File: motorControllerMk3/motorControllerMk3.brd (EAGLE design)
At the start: 100 x 80 mm, 39 parts, among them IC1 VNH3SP30, IC2 VNH3SP30

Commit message: deleted useless files, playing around with layout
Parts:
- moved R3 157.1 mm to (88.9, 6.35)
- moved SV2 146.4 mm to (87.6, 34.3)
- moved CN1 145.0 mm to (94.0, 72.4)
- moved R2 145.0 mm to (81.3, 6.35)
- moved C7 140.3 mm to (78.7, 72.4)
- moved C5 135.4 mm to (73.7, 6.35)
- moved C1 134.1 mm to (68.6, 73.7)
- moved C6 133.6 mm to (77.5, 50.8)
- moved LED5 124.1 mm to (68.6, 49.5)
- moved SV1 119.4 mm to (77.5, 43.2), turned to 180 degrees
- moved IC1 97.2 mm to (72.4, 21.6), turned to 270 degrees
- moved LED6 94.5 mm to (33.0, 74.9)
- moved R11 90.9 mm to (39.4, 64.8)
- moved Q1 85.6 mm to (52.1, 73.7)
- moved U$1 80.0 mm to (48.3, 44.5), turned to 180 degrees
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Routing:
- net +12V: track 0.00 -> 55.2 mm

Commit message: further layouting
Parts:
- moved R17 96.8 mm to (45.7, 21.6)
- moved R14 95.6 mm to (59.7, 21.6), turned to 180 degrees
- moved R13 92.7 mm to (59.7, 16.5), turned to 180 degrees
- moved R16 90.4 mm to (45.7, 26.7)
- moved R15 89.2 mm to (45.7, 16.5)
- moved R12 84.3 mm to (59.7, 26.7), turned to 180 degrees
- moved R5 75.0 mm to (45.7, 24.1)
- moved R10 73.8 mm to (58.4, 58.4)
- moved R4 73.3 mm to (45.7, 19.1)
- moved R3 31.9 mm to (59.7, 19.1), turned to 180 degrees
- moved R2 28.0 mm to (59.7, 24.1), turned to 180 degrees
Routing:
- net +5V: track 0.00 -> 25.4 mm, vias 0 -> 4
- net N$25: track 0.00 -> 18.1 mm
- net N$24: track 0.00 -> 18.1 mm
- net N$9: track 0.00 -> 12.4 mm
- net N$8: track 0.00 -> 12.4 mm
- net N$26: track 0.00 -> 6.04 mm
- net N$23: track 0.00 -> 6.03 mm
- net N$36: track 0.00 -> 3.80 mm
- net N$32: track 0.00 -> 3.80 mm
- net N$35: track 0.00 -> 3.80 mm
- net N$33: track 0.00 -> 3.80 mm
- net N$21: track 0.00 -> 2.97 mm
- net N$20: track 0.00 -> 2.97 mm
- net N$19: track 0.00 -> 2.97 mm
- net N$18: track 0.00 -> 2.97 mm
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
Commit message: finished layout
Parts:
- moved LED3 109.5 mm to (62.9, 33.0), turned to 180 degrees
- moved LED2 102.3 mm to (62.9, 36.8), turned to 180 degrees
- moved C4 102.3 mm to (56.5, 55.9)
- moved R9 100.6 mm to (57.1, 36.2), turned to 180 degrees
- moved R7 91.4 mm to (57.1, 33.7)
- moved R8 83.5 mm to (43.8, 33.7), turned to 180 degrees
- moved C7 74.3 mm to (36.2, 11.4), turned to 180 degrees
- moved R6 72.9 mm to (43.8, 36.8)
- moved LED1 72.9 mm to (38.1, 36.8)
- moved C3 70.1 mm to (50.2, 55.2)
- moved SV2 63.6 mm to (24.1, 38.1), turned to 270 degrees
- moved R1 57.4 mm to (33.0, 51.4)
- moved ISP1 55.3 mm to (37.5, 56.5), turned to 90 degrees
- moved C2 53.8 mm to (35.6, 48.3), turned to 90 degrees
- moved LED4 48.6 mm to (38.1, 33.0)
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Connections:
- net N$15: now also SV2.6; no longer SV2.5
- net N$16: now also SV2.5; no longer SV2.6
- net N$24: now also R12.2, U$1.28; no longer R15.2, U$1.22
- net N$25: now also R15.2; no longer R13.2
- net N$26: now also R13.2; no longer R12.2
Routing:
- net +5V: track 25.4 -> 166.6 mm, vias 4 -> 6
- net N$14: track 0.00 -> 36.2 mm, vias 0 -> 3
- net N$16: track 0.00 -> 36.2 mm, vias 0 -> 3
- net N$26: track 6.04 -> 42.2 mm
- net N$17: track 0.00 -> 31.9 mm, vias 0 -> 1
- net GND: track 0.00 -> 25.7 mm, vias 0 -> 1
- net N$12: track 0.00 -> 24.3 mm
- net N$5: track 0.00 -> 20.4 mm, vias 0 -> 1
- net +12V: track 55.2 -> 73.2 mm
- net N$25: track 18.1 -> 35.2 mm
- net N$1: track 0.00 -> 16.2 mm, vias 0 -> 2
- net N$8: track 12.4 -> 28.1 mm, vias 0 -> 2
- net N$6: track 0.00 -> 15.5 mm
- net N$7: track 0.00 -> 15.2 mm
- net N$9: track 12.4 -> 26.8 mm, vias 0 -> 2
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- added copper zone on layer 1, net GND
- added copper zone on layer 16, net GND
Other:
- board size 100 x 80 mm -> 61.3 x 63.5 mm

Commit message: finalizing layout
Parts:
- added S1: (no value), switch-omron:B3F-10XX
- moved C8 34.7 mm to (30.8, 37.8), turned to 90 degrees
- moved C4 8.26 mm to (64.1, 52.7)
- moved CN1 8.03 mm to (60.3, 59.7)
- moved ISP1 3.81 mm to (41.3, 56.5)
- moved LED6 1.91 mm to (69.2, 48.3)
- moved R11 1.91 mm to (69.2, 42.5)
- moved C3 1.42 mm to (51.4, 55.9), turned to 90 degrees
- moved C1 1.27 mm to (35.6, 45.7), turned to 0 degrees
- moved LED5 1.27 mm to (65.4, 48.3)
- moved R10 1.27 mm to (65.4, 42.5)
- moved C2 0.63 mm to (35.6, 47.6), turned to 180 degrees
- moved C7 0.63 mm to (35.6, 11.4)
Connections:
- removed net N$5: ISP1.5, R1.2, U$1.13
- new net N$38: ISP1.5, R1.2, S1.1, S1.2, U$1.13
- net GND: now also S1.3, S1.4
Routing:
- net N$38: track 0.00 -> 33.0 mm, vias 0 -> 1
- net N$5: track 20.4 -> 0.00 mm, vias 1 -> 0
- net +12V: track 73.2 -> 87.7 mm
- net +5V: track 166.6 -> 172.8 mm
- net N$6: track 15.5 -> 10.7 mm
- net N$10: track 6.78 -> 11.4 mm
- net N$11: track 6.78 -> 11.4 mm
- net N$7: track 15.2 -> 11.1 mm
- net N$1: track 16.2 -> 12.4 mm
- net N$4: track 4.67 -> 3.36 mm
- net N$2: track 11.6 -> 10.5 mm
- net N$12: track 24.3 -> 23.3 mm
- net N$3: track 11.4 -> 10.5 mm
- net GND: vias 1 -> 16
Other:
- board size 61.3 x 63.5 mm -> 61.6 x 54.6 mm

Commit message: finalizing layout
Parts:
- removed CN1: (no value), adafruit:USB-MINIB
- removed IC1, IC2: VNH3SP30, st-microelectronics:MULTIPOWERSO-30
- removed ISP1: AVRISP-6, adafruit:AVRISP
- removed Q1: (no value), adafruit:HC49U-V
- removed S1: (no value), switch-omron:B3F-10XX
- removed SV1, SV2: (no value), con-lstb:MA06-1
- added C9: 2200u, rcl:E5-8,5
- added J1: AVR_SPI_PRG_6NS, SparkFun-Connectors:2X3-NS
- added JP1, JP2: (no value), SparkFun-Connectors:1X06
- added JP3: USB-SMD-NS, SparkFun-Connectors:USB-MINIB-NOSTOP
- added S2: SWITCH-MOMENTARY-2PTH, SparkFun-Electromechanical:TACTILE-PTH
- added U$2: ATMEGA32U4TQFP, SparkFun-DigitalIC:SPARKFUN-DIGITALIC_TQFP44
- added U$3: VNH2SP30, SparkFun-PowerIC:VNH2SP30
- added Y1: (no value), SparkFun-FreqCtrl:HC49US
- C1, C2, C3, C4, C5, C6, C7: device rcl:C0805K -> SparkFun-Passives:0805
- LED1: value (none) -> A2; device led:SML1206 -> SparkFun-LED:LED-1206
- LED2: value (none) -> B1; device led:SML1206 -> SparkFun-LED:LED-1206
- LED3: value (none) -> A1; device led:SML1206 -> SparkFun-LED:LED-1206
- LED4: value (none) -> B2; device led:SML1206 -> SparkFun-LED:LED-1206
- LED5: value (none) -> +5V; device led:SML1206 -> SparkFun-LED:LED-1206
- LED6: value (none) -> +12V; device led:SML1206 -> SparkFun-LED:LED-1206
- R1: value (none) -> 10k; device rcl:M0805 -> SparkFun-Passives:0805
- R10, R11, R12, R13, R14, R15, R16, R17, R2, R3, R4, R5, R6, R7, R8, R9: device rcl:M0805 -> SparkFun-Passives:0805
- U$1: value ATMEGA32U4-AU -> VNH2SP30; device adafruit:TQFP44 -> SparkFun-PowerIC:VNH2SP30
- moved U$1 30.0 mm to (33.7, 21.6), turned to 90 degrees
- moved LED6 9.53 mm to (74.9, 55.9), turned to 90 degrees
- moved LED5 9.16 mm to (70.5, 55.9), turned to 90 degrees
- moved R10 8.25 mm to (68.6, 50.2)
- moved R11 8.25 mm to (72.4, 50.2)
- moved R1 3.42 mm to (36.2, 52.7), turned to 270 degrees
- moved C5 3.18 mm to (61.0, 42.5), turned to 0 degrees
- moved LED1 1.91 mm to (40.0, 36.8), turned to 180 degrees
- moved LED2 1.91 mm to (61.0, 36.8), turned to 0 degrees
- moved LED3 1.91 mm to (61.0, 33.0), turned to 0 degrees
- moved LED4 1.91 mm to (40.0, 33.0), turned to 180 degrees
- moved C3 1.42 mm to (52.7, 55.2), turned to 0 degrees
- moved C4 1.27 mm to (64.1, 51.4)
- moved R9 0.90 mm to (56.5, 36.8)
- moved C6 0.64 mm to (64.8, 11.4)
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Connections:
- removed net N$14: IC1.15, IC1.16, IC1.21, IC1.OUTB, IC1.OUTB@1, SV1.5
- removed net N$15: IC2.15, IC2.16, IC2.21, IC2.OUTB, IC2.OUTB@1, SV2.6
- removed net N$16: IC2.1, IC2.25, IC2.30, IC2.OUTA, IC2.OUTA@1, SV2.5
- removed net N$18: IC2.6, R4.1
- removed net N$19: IC2.10, R5.1
- removed net N$21: IC1.10, R3.1
- removed net N$23: R16.2, R8.1, U$1.25
- removed net N$24: R12.2, R7.1, U$1.28
- removed net N$25: R15.2, R6.2, U$1.26
- removed net N$26: R13.2, R9.2, U$1.27
- removed net N$32: IC1.5, R12.1
- removed net N$33: IC1.11, R13.1
- removed net N$34: IC1.8, R14.1
- removed net N$35: IC2.5, R15.1
- removed net N$36: IC2.11, R16.1
- removed net N$37: IC2.8, R17.1
- new net N$5: R16.1, U$1.11
- new net OUTA1: JP1.1, U$3.1, U$3.25, U$3.30, U$3.SLUG3
- new net OUTA2: JP2.2, U$1.1, U$1.25, U$1.30, U$1.SLUG3
- new net OUTB1: JP1.2, U$3.15, U$3.16, U$3.21, U$3.SLUG2
- new net OUTB2: JP2.1, U$1.15, U$1.16, U$1.21, U$1.SLUG2
- new net PB0: U$2.8
- new net PB1: J1.3, U$2.9
- new net PB2: J1.4, U$2.10
- new net PB3: J1.1, U$2.11
- new net PB4: R12.2, R7.1, U$2.28
- new net PB5: R17.2, U$2.29
- new net PB6: R14.2, U$2.30
- new net PB7: U$2.12
- new net PC6: U$2.31
- new net PC7: U$2.32
- new net PD0: JP2.6, U$2.18
- new net PD1: JP1.6, U$2.19
- new net PD2: U$2.20
- new net PD3: U$2.21
- new net PD4: R16.2, R8.1, U$2.25
- new net PD5: U$2.22
- new net PD6: R15.2, R6.2, U$2.26
- new net PD7: R13.2, R9.2, U$2.27
- new net PE6: U$2.1
- net +12V: now also C9.+, U$1.13, U$1.23, U$1.3, U$1.SLUG1, U$3.13, U$3.23, U$3.3, U$3.SLUG1; no longer IC1.13, IC1.23, IC1.3, IC1.VCC, IC1.VCC@1, IC2.13, IC2.23, IC2.3, IC2.VCC, IC2.VCC@1
- net +5V: now also J1.2, JP1.4, JP2.4, JP3.VBUS, U$2.14, U$2.2, U$2.24, U$2.34, U$2.44, U$2.7; no longer CN1.VBUS, ISP1.2, SV1.3, SV2.3, U$1.14, U$1.2, U$1.24, U$1.34, U$1.44, U$1.7
- net GND: now also C9.-, J1.6, JP1.3, JP2.3, JP3.GND, S2.1, U$1.18, U$1.19, U$1.20, U$1.26, U$1.27, U$1.28, U$2.15, U$2.23, U$2.35, U$2.43, U$2.5, U$3.18, U$3.19, U$3.20, U$3.26, U$3.27, U$3.28; no longer CN1.GND, IC1.18, IC1.19, IC1.20, IC1.26, IC1.27, IC1.28, IC2.18, IC2.19, IC2.20, IC2.26, IC2.27, IC2.28, ISP1.6, S1.3, S1.4, SV1.4, SV2.4, U$1.15, U$1.23, U$1.35, U$1.43, U$1.5
- net N$1: now also R15.1, U$1.5; no longer ISP1.3, U$1.9
- net N$10: now also JP3.D+, U$2.4; no longer CN1.D+, U$1.4
- net N$11: now also JP3.D-, U$2.3; no longer CN1.D-, U$1.3
- net N$12: now also R13.1, U$3.11; no longer SV2.1, U$1.18
- net N$13: now also R14.1, U$3.8; no longer IC1.1, IC1.25, IC1.30, IC1.OUTA, IC1.OUTA@1, SV1.6
- net N$17: now also R3.1, U$3.10; no longer SV1.1, U$1.19
- net N$2: now also U$2.16, Y1.1; no longer Q1.1, U$1.16
- net N$20: now also U$3.6; no longer IC1.6
- net N$3: now also U$2.17, Y1.2; no longer Q1.2, U$1.17
- net N$38: now also J1.5, S2.3, U$2.13; no longer ISP1.5, S1.1, S1.2, U$1.13
- net N$4: now also U$2.6; no longer U$1.6
- net N$6: now also R17.1, U$1.8; no longer ISP1.4, U$1.10
- net N$7: now also R5.1, U$1.10; no longer ISP1.1, U$1.11
- net N$8: now also R4.1, U$1.6; no longer R17.2, U$1.29
- net N$9: now also R12.1, U$3.5; no longer R14.2, U$1.30
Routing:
- net OUTA2: track 0.00 -> 85.4 mm, vias 0 -> 6
- net OUTB1: track 0.00 -> 83.7 mm, vias 0 -> 6
- net +12V: track 87.7 -> 166.6 mm, vias 0 -> 4
- net N$26: track 42.2 -> 0.00 mm
- net PD7: track 0.00 -> 41.8 mm
- net OUTB2: track 0.00 -> 39.9 mm
- net OUTA1: track 0.00 -> 39.9 mm
- net N$14: track 36.2 -> 0.00 mm, vias 3 -> 0
- net N$16: track 36.2 -> 0.00 mm, vias 3 -> 0
- net N$25: track 35.2 -> 0.00 mm
- net PD6: track 0.00 -> 35.0 mm
- net PD1: track 0.00 -> 31.0 mm, vias 0 -> 1
- net N$17: track 31.9 -> 2.65 mm, vias 1 -> 0
- net PB5: track 0.00 -> 28.1 mm, vias 0 -> 2
- net PB6: track 0.00 -> 26.8 mm, vias 0 -> 2
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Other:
- board size 61.6 x 54.6 mm -> 57.1 x 52.7 mm
- board text added: "+12V"
- board text added: "GND"
- board text added: "ISP"
- board text added: "RESET"

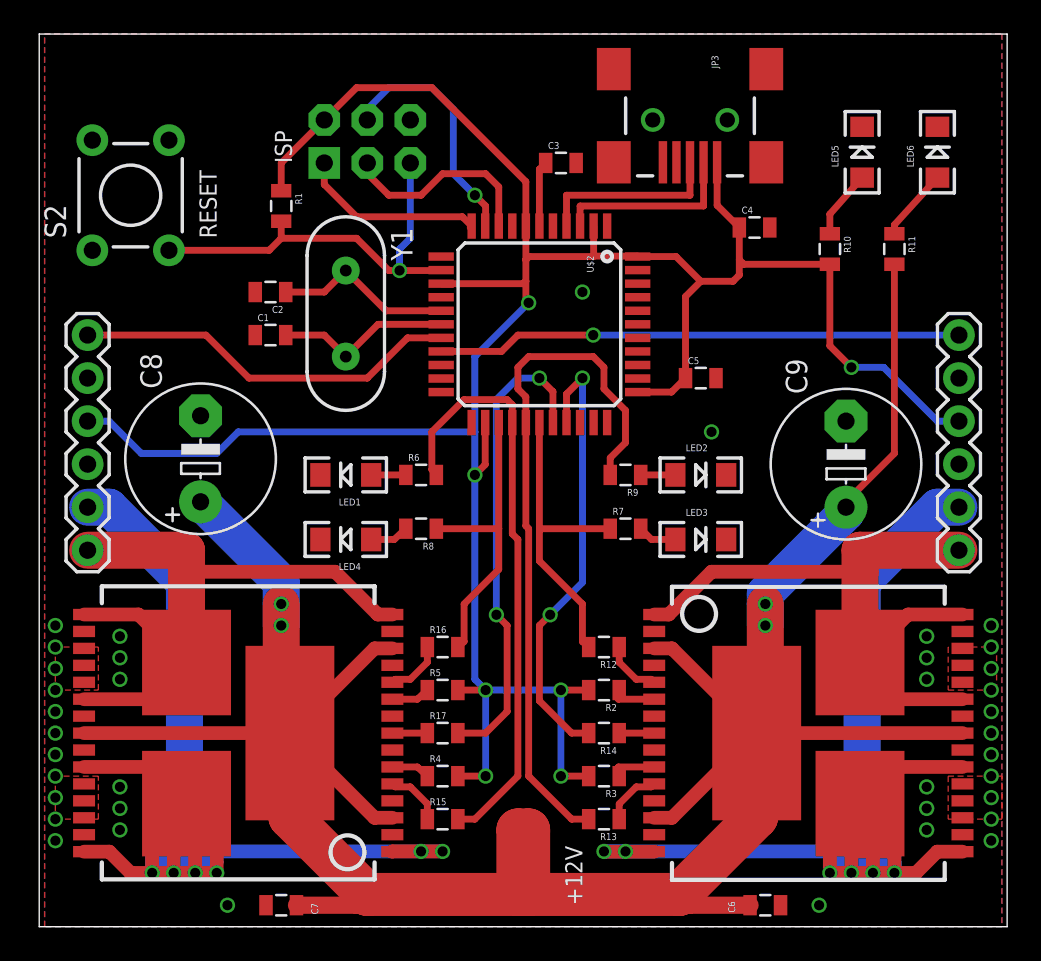
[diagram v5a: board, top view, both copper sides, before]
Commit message: now fits onto 5x10 cm pcb
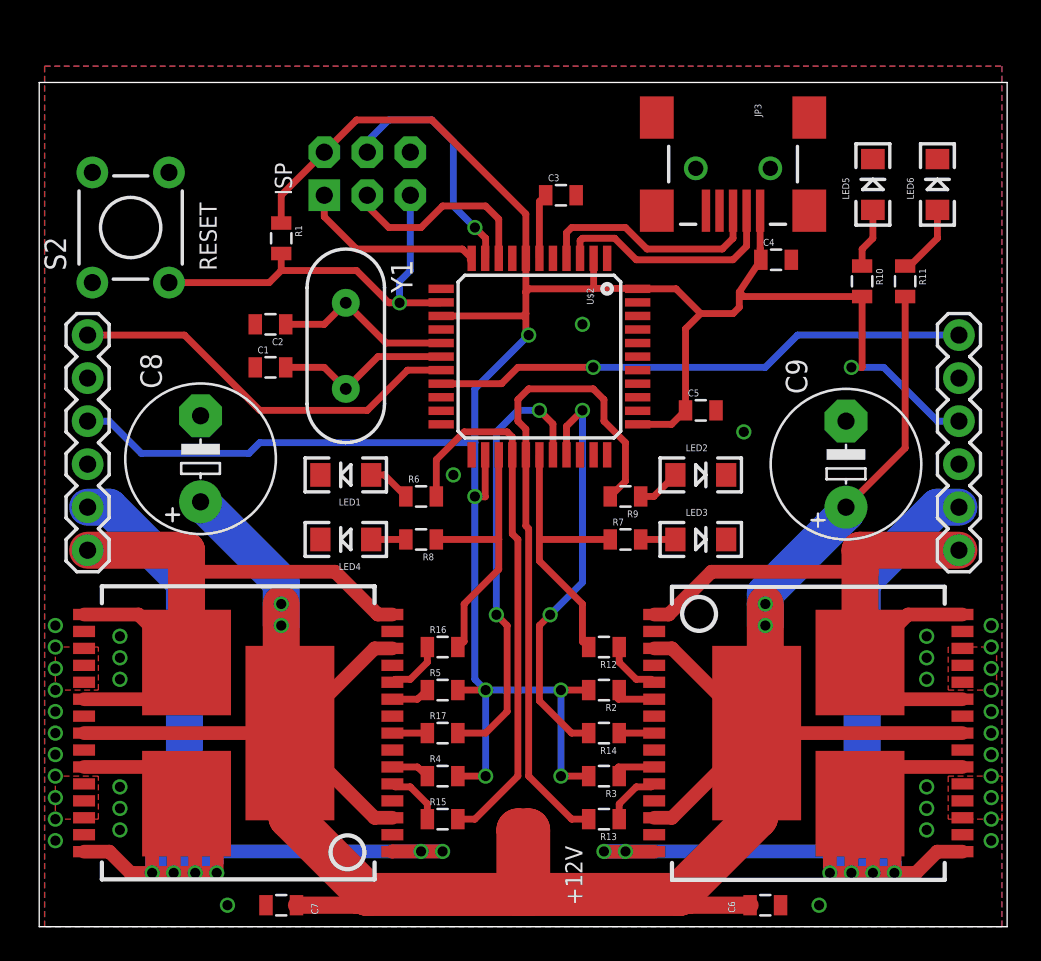
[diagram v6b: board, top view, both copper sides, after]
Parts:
- moved JP3 3.82 mm to (62.9, 54.9)
- moved R10 2.69 mm to (70.5, 48.3)
- moved C4 2.29 mm to (65.4, 49.5)
- moved LED5 2.01 mm to (71.1, 54.0)
- moved R11 2.01 mm to (73.0, 48.3)
- moved C1 1.91 mm to (35.6, 43.2)
- moved C2 1.91 mm to (35.6, 45.7)
- moved C5 1.91 mm to (61.0, 40.6)
- moved J1 1.91 mm to (41.3, 54.6)
- moved LED6 1.91 mm to (74.9, 54.0)
- moved R1 1.91 mm to (36.2, 50.8)
- moved S2 1.91 mm to (27.3, 51.4)
- moved U$2 1.91 mm to (51.4, 43.8)
- moved C3 1.90 mm to (52.7, 53.3)
- moved Y1 1.90 mm to (40.0, 44.5)
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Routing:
- net +5V: track 157.0 -> 153.6 mm
- net N$10: track 11.1 -> 13.9 mm
- net N$11: track 11.1 -> 13.9 mm
- net PD6: track 35.0 -> 32.2 mm
- net PD7: track 41.8 -> 39.3 mm
- net PD4: track 18.0 -> 16.0 mm
- net PB6: track 26.8 -> 24.9 mm
- net PB4: track 18.7 -> 16.7 mm
- net PB5: track 28.1 -> 26.2 mm
- net +12V: track 166.6 -> 165.0 mm
- net PD0: track 22.9 -> 23.7 mm
- net PD1: track 31.0 -> 31.8 mm
- net N$31: track 2.04 -> 2.57 mm
- net N$30: track 2.05 -> 2.57 mm
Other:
- board size 57.1 x 52.7 mm -> 57.1 x 49.8 mm

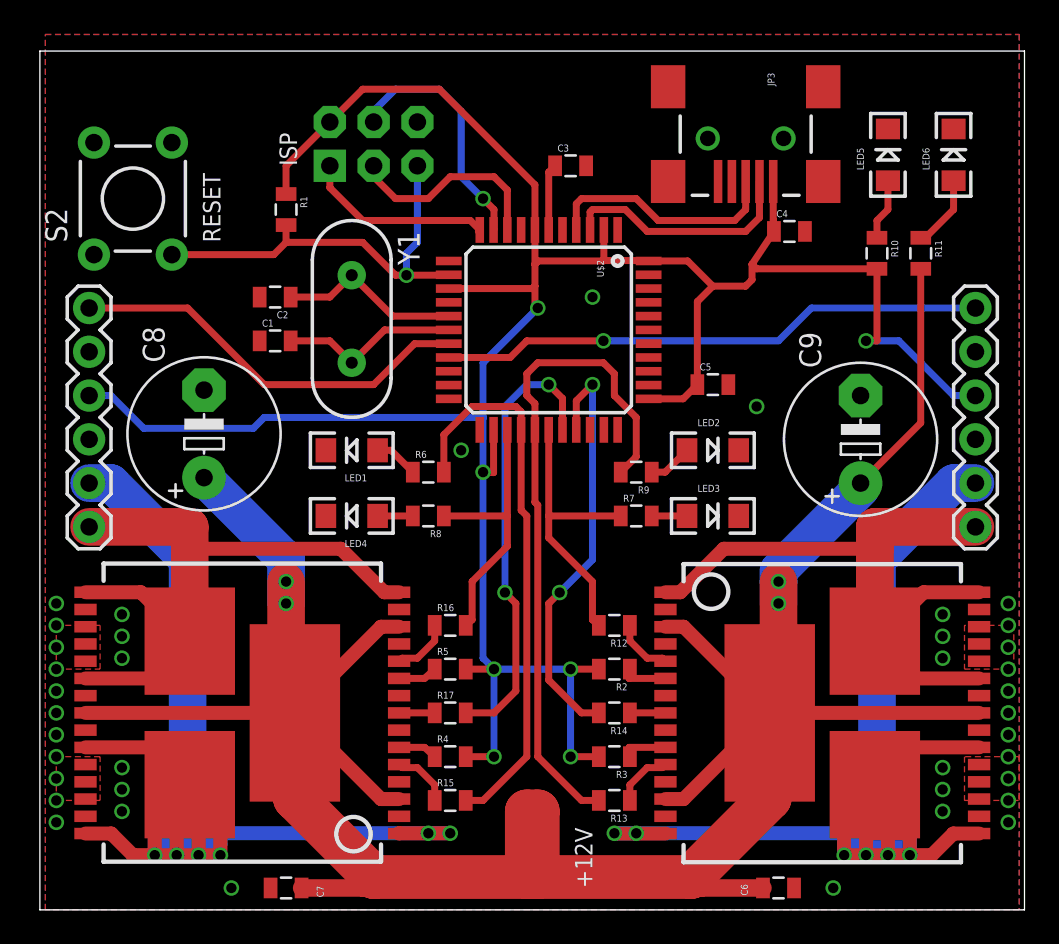
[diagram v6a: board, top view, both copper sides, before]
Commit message: making pcb smaller
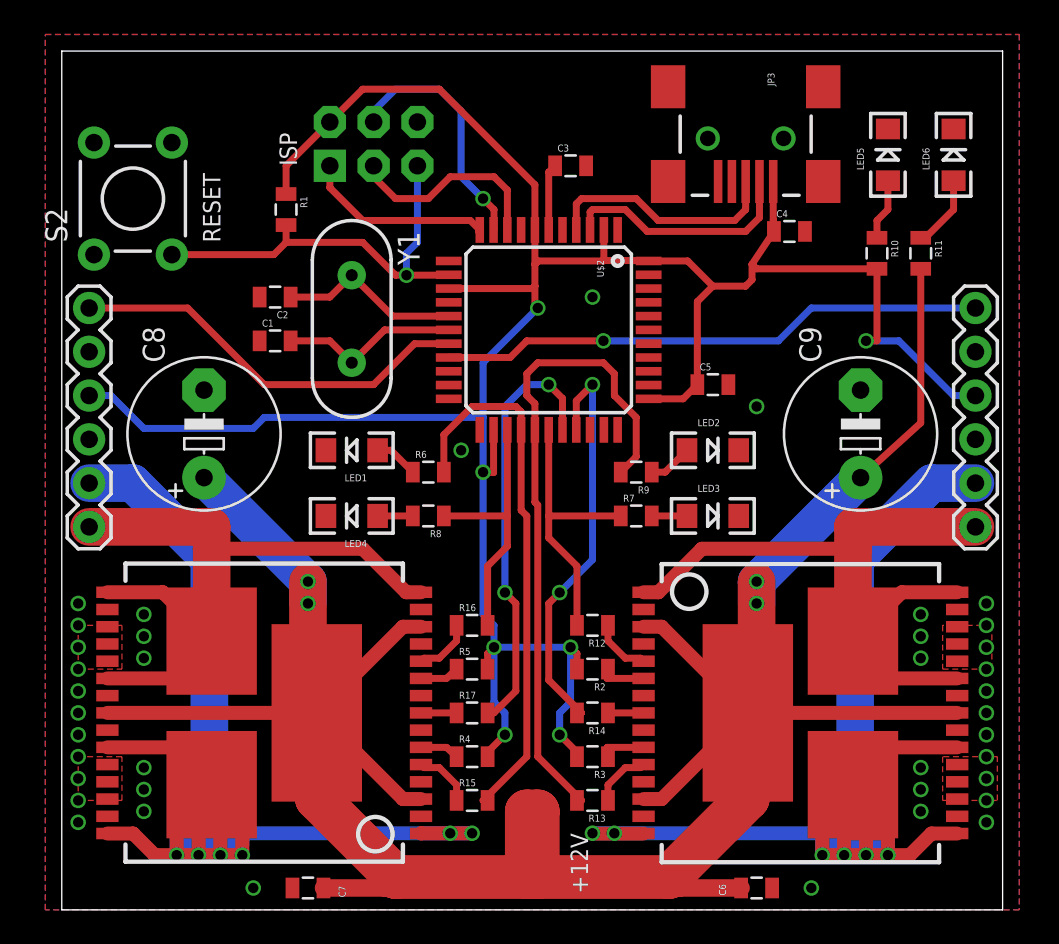
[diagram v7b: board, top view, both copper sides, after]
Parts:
- moved C7 1.27 mm to (37.5, 11.4)
- moved R15 1.27 mm to (47.0, 16.5)
- moved R16 1.27 mm to (47.0, 26.7)
- moved R17 1.27 mm to (47.0, 21.6)
- moved R4 1.27 mm to (47.0, 19.1)
- moved R5 1.27 mm to (47.0, 24.1)
- moved C6 1.27 mm to (63.5, 11.4)
- moved R12 1.27 mm to (54.0, 26.7)
- moved R13 1.27 mm to (54.0, 16.5)
- moved R14 1.27 mm to (54.0, 21.6)
- moved R2 1.27 mm to (54.0, 24.1)
- moved R3 1.27 mm to (54.0, 19.1)
- moved U$1 1.27 mm to (34.9, 21.6)
- moved U$3 1.27 mm to (66.0, 21.6)
- moved C9 0.32 mm to (69.5, 37.8)
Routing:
- net +12V: track 165.0 -> 163.6 mm
- net OUTA2: track 85.4 -> 86.6 mm
- net PB5: track 26.2 -> 25.0 mm
- net OUTA1: track 39.9 -> 41.1 mm
- net OUTB2: track 39.9 -> 41.1 mm
- net OUTB1: track 83.7 -> 85.0 mm
- net +5V: track 153.6 -> 152.5 mm
- net PD6: track 32.2 -> 31.5 mm
- net PD7: track 39.3 -> 38.6 mm
- net PB6: track 24.9 -> 24.2 mm
- net PD4: track 16.0 -> 15.5 mm
- net PB4: track 16.7 -> 16.2 mm
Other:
- board size 57.1 x 49.8 mm -> 54.6 x 49.8 mm
